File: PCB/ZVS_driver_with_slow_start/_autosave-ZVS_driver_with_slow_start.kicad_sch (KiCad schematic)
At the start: 31 parts, among them J1 Battery_12v_Connection, J2 Power_Switch, J3 ON_switch, J4 Conn_01x02_Socket, Q1 IRF640NPbF, Q2 IRF640NPbF, Q3 IRF640NPbF, U1 OP07, U2 OP07

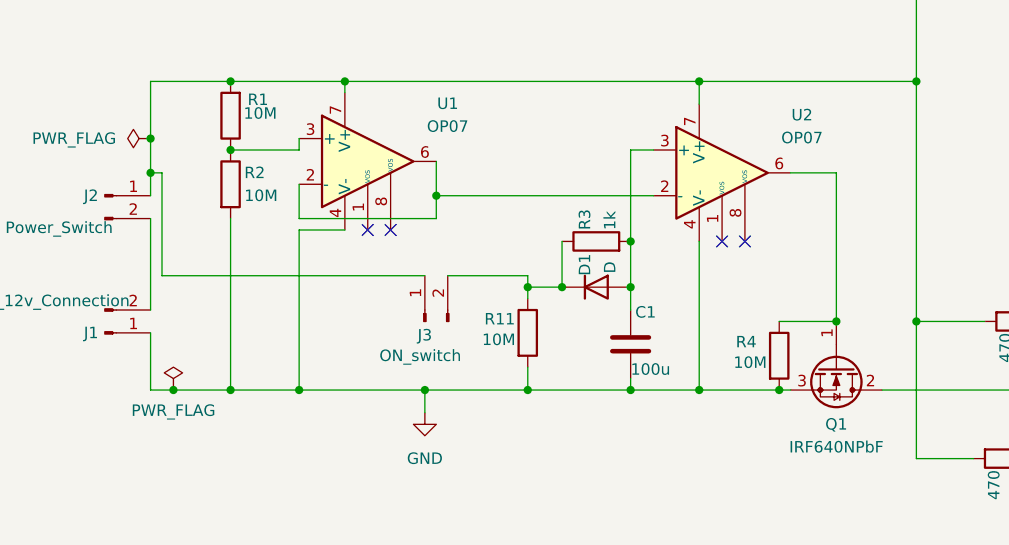
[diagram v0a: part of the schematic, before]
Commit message: added curent limiting RL on Q1
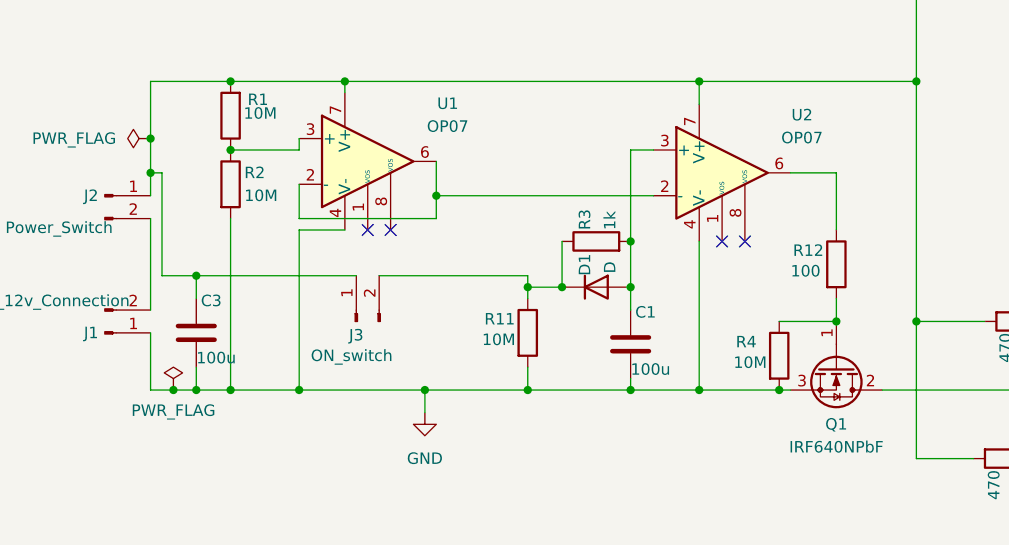
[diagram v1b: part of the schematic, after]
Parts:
- added C3: 100u, Capacitor_SMD:C_0805_2012Metric, symbol Device:C
- added R12: 100, Resistor_SMD:R_0805_2012Metric, symbol Device:R
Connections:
- net GND: now also C3.2
- net at D3.1 (K), D4.1 (K), J2.1 (Pin_1)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: now also C3.1
- net at Q1.1 (G), R4.1: now also R12.2; no longer U2.6
- new net: R12.1, U2.6
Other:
- moved on the sheet: J3
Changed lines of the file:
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@@
+	)
+	(junction
+		(at 48.26 100.33)
+		(diameter 0)
+		(color 0 0 0 0)
 	)
 	(junction
@@
 	(junction
 		(at 43.18 85.09)
+		(diameter 0)
+		(color 0 0 0 0)
+	)
+	(junction
+		(at 48.26 113.03)
 		(diameter 0)
 		(color 0 0 0 0)
@@
 	(wire
 		(pts
-			(xy 119.38 88.9) (xy 119.38 105.41)
+			(xy 119.38 88.9) (xy 119.38 95.25)
 		)
 		(stroke
@@
 	(wire
 		(pts
+			(xy 119.38 102.87) (xy 119.38 105.41)
+		)
+		(stroke
+			(width 0)
+			(type default)
+		)
+	)
+	(wire
+		(pts
 			(xy 187.96 68.58) (xy 187.96 66.04)
 		)
@@
 	(wire
 		(pts
+			(xy 48.26 113.03) (xy 48.26 110.49)
+		)
+		(stroke
+			(width 0)
+			(type default)
+		)
+	)
+	(wire
+		(pts
 			(xy 43.18 93.98) (xy 43.18 104.14)
 		)
@@
 	(wire
 		(pts
+			(xy 48.26 113.03) (xy 52.07 113.03)
+		)
+		(stroke
+			(width 0)
+			(type default)
+		)
+	)
+	(wire
+		(pts
 			(xy 85.09 113.03) (xy 96.52 113.03)
 		)
@@
 	(wire
 		(pts
-			(xy 45.72 113.03) (xy 52.07 113.03)
+			(xy 45.72 113.03) (xy 48.26 113.03)
 		)
 		(stroke
@@
 	(wire
 		(pts
+			(xy 48.26 102.87) (xy 48.26 100.33)
+		)
+		(stroke
+			(width 0)
+			(type default)
+		)
+	)
+	(wire
+		(pts
 			(xy 104.14 113.03) (xy 113.03 113.03)
 		)
@@
 	(wire
 		(pts
-			(xy 76.2 100.33) (xy 85.09 100.33)
+			(xy 48.26 100.33) (xy 66.04 100.33)
+		)
+		(stroke
+			(width 0)
+			(type default)
+		)
+	)
+	(wire
+		(pts
+			(xy 68.58 100.33) (xy 85.09 100.33)
 		)
 		(stroke
@@
 	(wire
 		(pts
-			(xy 73.66 100.33) (xy 44.45 100.33)
+			(xy 44.45 100.33) (xy 48.26 100.33)
 		)
 		(stroke
@@
 	)
 	(symbol
+		(lib_id "Device:C")
+		(at 48.26 106.68 0)
+		(unit 1)
+		(exclude_from_sim no)
+		(in_bom yes)
+		(on_board yes)
+		(dnp no)
+		(property "Reference" "C3"
+			(at 48.768 103.124 0)
+			(effects
+				(font
+					(size 1.27 1.27)
+				)
+				(justify left)
+			)
+		)
+		(property "Value" "100u"
+			(at 48.26 109.474 0)
+			(effects
+				(font
+					(size 1.27 1.27)
+				)
+				(justify left)
+			)
+		)
+		(property "Footprint" "Capacitor_SMD:C_0805_2012Metric"
+			(at 49.2252 110.49 0)
+			(effects
+				(font
+					(size 1.27 1.27)
+				)
+				(hide yes)
+			)
+		)
+		(property "Datasheet" "~"
+			(at 48.26 106.68 0)
+			(effects
+				(font
+					(size 1.27 1.27)
+				)
+				(hide yes)
+			)
+		)
+		(property "Description" "Unpolarized capacitor"
+			(at 48.26 106.68 0)
+			(effects
+				(font
+					(size 1.27 1.27)
+				)
+				(hide yes)
+			)
+		)
+		(pin "2"
+		)
+		(pin "1"
+		)
+		(instances
+			(project "ZVS_driver_with_slow_start"
+				(path "/c49e841c-fad0-4812-b9c2-9ea62c8990ee"
+					(reference "C3")
+					(unit 1)
+				)
+			)
+		)
+	)
+	(symbol
 		(lib_id "Connector:Conn_01x02_Socket")
 		(at 224.79 111.76 0)
@@
 	(symbol
 		(lib_id "Connector:Conn_01x02_Pin")
-		(at 73.66 105.41 90)
+		(at 66.04 105.41 90)
 		(unit 1)
 		(exclude_from_sim no)
@@
 		(dnp no)
 		(property "Reference" "J3"
-			(at 73.66 106.934 90)
+			(at 66.04 106.934 90)
 			(effects
 				(font
@@
 		)
 		(property "Value" "ON_switch"
-			(at 73.152 109.22 90)
+			(at 65.532 109.22 90)
 			(effects
 				(font
@@
 		)
 		(property "Footprint" "Connector_AMASS:AMASS_XT30U-F_1x02_P5.0mm_Vertical"
-			(at 73.66 105.41 0)
+			(at 66.04 105.41 0)
 			(effects
 				(font
@@
 		)
 		(property "Datasheet" "~"
-			(at 73.66 105.41 0)
+			(at 66.04 105.41 0)
 			(effects
 				(font
@@
 		)
 		(property "Description" "Generic connector, single row, 01x02, script generated"
-			(at 73.66 105.41 0)
+			(at 66.04 105.41 0)
 			(effects
 				(font
@@
 					(unit 1)
 				)
+			)
+		)
+	)
+	(symbol
+		(lib_id "Device:R")
+		(at 119.38 99.06 0)
+		(unit 1)
+		(exclude_from_sim no)
+		(in_bom yes)
+		(on_board yes)
+		(dnp no)
+		(property "Reference" "R12"
+			(at 114.554 97.536 0)
+			(effects
+				(font
+					(size 1.27 1.27)
+				)
+				(justify left)
+			)
+		)
+		(property "Value" "100"
+			(at 114.3 99.822 0)
+			(effects
+				(font
+					(size 1.27 1.27)
+				)
+				(justify left)
+			)
+		)
+		(property "Footprint" "Resistor_SMD:R_0805_2012Metric"
+			(at 117.602 99.06 90)
+			(effects
+				(font
+					(size 1.27 1.27)
+				)
+				(hide yes)
+			)
+		)
+		(property "Datasheet" "~"
+			(at 119.38 99.06 0)
+			(effects
+				(font
+					(size 1.27 1.27)
+				)
+				(hide yes)
+			)
+		)
+		(property "Description" "Resistor"
+			(at 119.38 99.06 0)
+			(effects
+				(font
+					(size 1.27 1.27)
+				)
+				(hide yes)
+			)
+		)
+		(pin "1"
+		)
+		(pin "2"
+		)
+		(instances
+			(project "ZVS_driver_with_slow_start"
+				(path "/c49e841c-fad0-4812-b9c2-9ea62c8990ee"
+					(reference "R12")
+					(unit 1)
+				)
